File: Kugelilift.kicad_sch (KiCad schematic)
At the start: 14 parts, among them J1 I2C, J2 TTL, J4 Stepper, SW1 RESET, SW2 MODE, U1 magnetic-charger, U2 TCRT5000, U3 ULN2003A, U4 esp-01f, U5 UA78M33_TO252

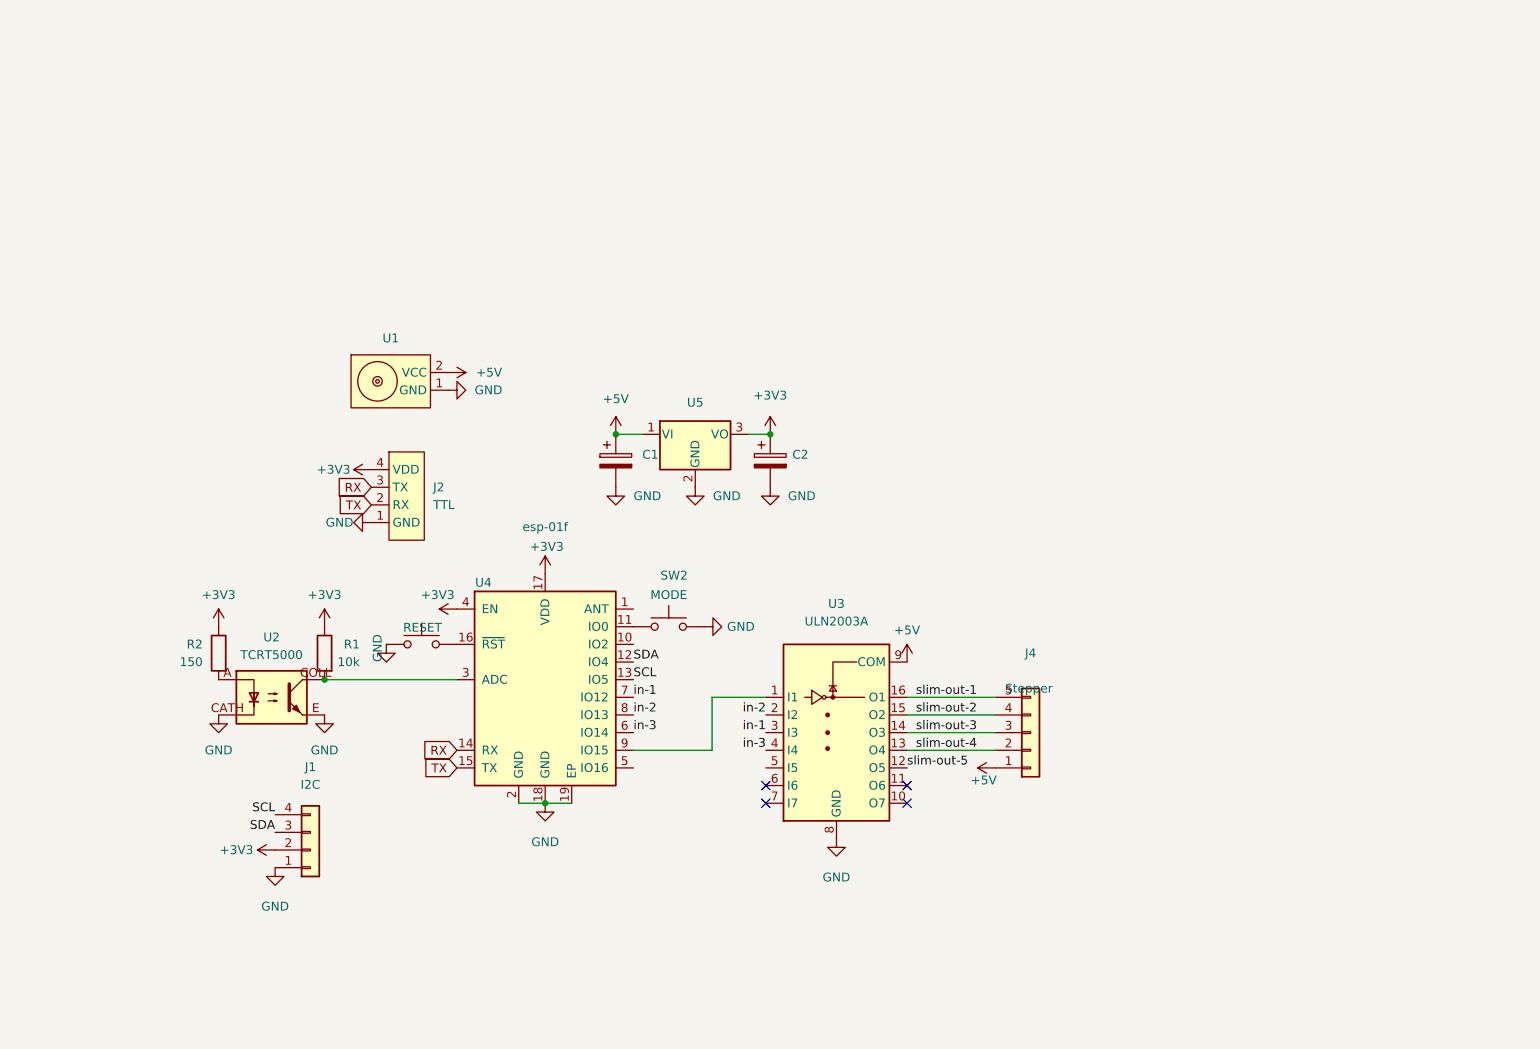
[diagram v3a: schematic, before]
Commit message: PCB based on ESP01m
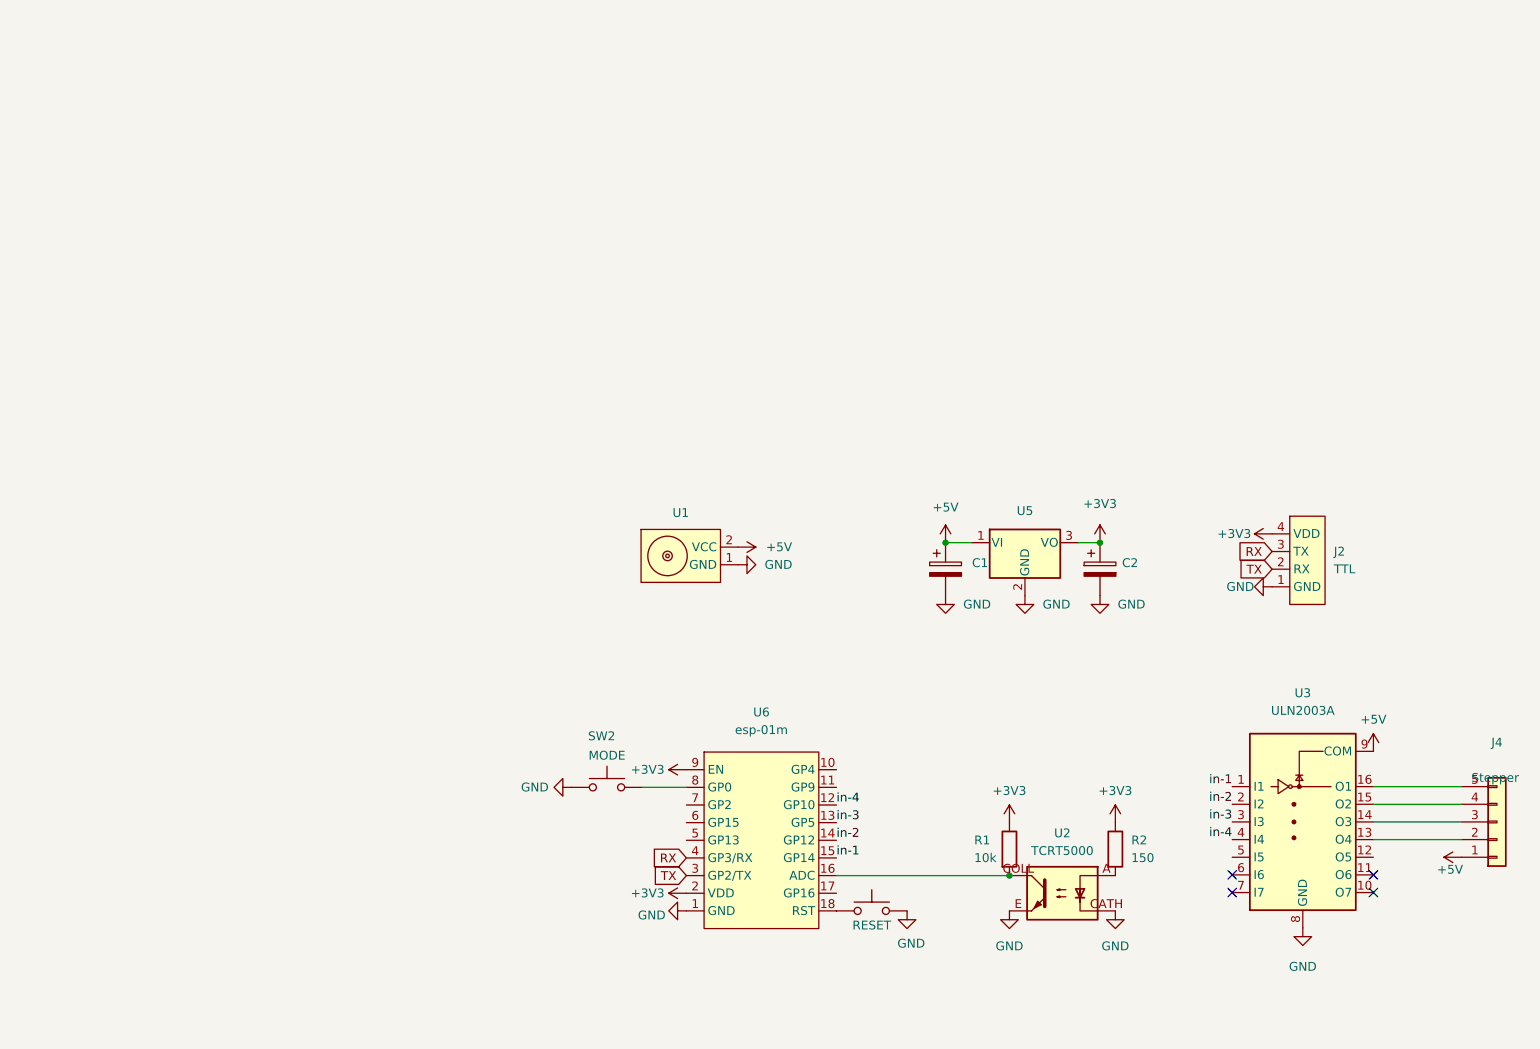
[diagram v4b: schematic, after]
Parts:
- removed J1: I2C, Connector_PinHeader_2.54mm:PinHeader_1x04_P2.54mm_Vertical, symbol Connector_Generic:Conn_01x04
- removed U4: esp-01f, esp-01f:esp-01f, symbol esp-01f:esp-01f
- added U6: esp-01m, esp-01m:esp-01m, symbol esp-01m:esp-01m
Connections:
- net +3V3: now also U6.2 (VDD), U6.9 (EN)
- net GND: now also U6.1 (GND)
- net RX: now also U6.4 (GP3/RX)
- net TX: now also U6.3 (GP2/TX)
- net in-1: now also U3.1 (I1), U6.15 (GP14); no longer U3.3 (I3)
- net in-2: now also U6.14 (GP12)
- net in-3: now also U3.3 (I3), U6.13 (GP5); no longer U3.4 (I4)
- net at SW2.1: now also U6.8 (GP0)
- net at SW1.1: now also U6.18 (RST)
- net at R1.2, U2.COLL: now also U6.16 (ADC)
- net slim-out-1: no longer names the net of J4.5 (Pin_5), U3.16 (O1)
- net slim-out-2: no longer names the net of J4.4 (Pin_4), U3.15 (O2)
- net slim-out-3: no longer names the net of J4.3 (Pin_3), U3.14 (O3)
- net slim-out-4: no longer names the net of J4.2 (Pin_2), U3.13 (O4)
- net slim-out-5: no longer names the net of U3.12 (O5)
- new net in-4: U3.4 (I4), U6.12 (GP10)
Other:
- moved on the sheet: C1, C2, J2, J4, R1, R2, SW2, U1, U2, U3, U5

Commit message: Prepare for next iteration
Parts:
- added SW3, SW?: SW_Push, Button_Switch_SMD:SW_Push_1P1T_NO_CK_KMR2, symbol Switch:SW_Push
- added SW4: SW_DIP_x04, Button_Switch_THT:SW_DIP_SPSTx04_Slide_6.7x11.72mm_W7.62mm_P2.54mm_LowProfile, symbol Switch:SW_DIP_x04
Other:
- note added: "TODOS: - Two user buttons for manual operation or configuration at startup - IR Receiver mode for use with a remote control. (needs a POC) - DIP Switches on the underside for configuration / wifi-enable etc. - Battery module adapter using magnetic sockets + uart (i2c)"
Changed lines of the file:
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@@
     (stroke (width 0) (type default) (color 0 0 0 0))
+  )
+  (text "TODOS:\n\n- Two user buttons for manual operation or configuration at startup\n- IR Receiver mode for use with a remote control. (needs a POC)\n- DIP Switches on the underside for configuration / wifi-enable etc.\n- Battery module adapter using magnetic sockets + uart (i2c)"
+    (at 33.02 93.98 0)
+    (effects (font (size 1.27 1.27)) (justify left bottom))
   )
   (label "in-4" (at 191.5668 129.4384 180)
@@
     (pin "1")
   )
+  (symbol (lib_id "Switch:SW_Push") (at 35.56 120.65 0) (unit 1)
+    (in_bom yes) (on_board yes) (fields_autoplaced)
+    (property "Reference" "SW3" (id 0) (at 35.56 113.03 0))
+    (property "Value" "SW_Push" (id 1) (at 35.56 115.57 0))
+    (property "Footprint" "Button_Switch_SMD:SW_Push_1P1T_NO_CK_KMR2" (id 2) (at 35.56 115.57 0)
+      (effects (font (size 1.27 1.27)) hide)
+    )
+    (property "Datasheet" "~" (id 3) (at 35.56 115.57 0)
+      (effects (font (size 1.27 1.27)) hide)
+    )
+    (pin "1")
+    (pin "2")
+  )
   (symbol (lib_id "power:GND") (at 120.4722 89.8906 90) (unit 1)
     (in_bom yes) (on_board yes) (fields_autoplaced)
@@
     )
     (pin "1")
+  )
+  (symbol (lib_id "Switch:SW_Push") (at 35.56 133.35 0) (unit 1)
+    (in_bom yes) (on_board yes) (fields_autoplaced)
+    (property "Reference" "SW?" (id 0) (at 35.56 125.73 0))
+    (property "Value" "SW_Push" (id 1) (at 35.56 128.27 0))
+    (property "Footprint" "Button_Switch_SMD:SW_Push_1P1T_NO_CK_KMR2" (id 2) (at 35.56 128.27 0)
+      (effects (font (size 1.27 1.27)) hide)
+    )
+    (property "Datasheet" "~" (id 3) (at 35.56 128.27 0)
+      (effects (font (size 1.27 1.27)) hide)
+    )
+    (pin "1")
+    (pin "2")
   )
   (symbol (lib_id "Device:C_Polarized") (at 172.5422 90.5256 0) (unit 1)
@@
     (pin "1")
   )
+  (symbol (lib_id "Switch:SW_DIP_x04") (at 72.39 152.4 0) (unit 1)
+    (in_bom yes) (on_board yes) (fields_autoplaced)
+    (property "Reference" "SW4" (id 0) (at 72.39 139.7 0))
+    (property "Value" "SW_DIP_x04" (id 1) (at 72.39 142.24 0))
+    (property "Footprint" "Button_Switch_THT:SW_DIP_SPSTx04_Slide_6.7x11.72mm_W7.62mm_P2.54mm_LowProfile" (id 2) (at 72.39 152.4 0)
+      (effects (font (size 1.27 1.27)) hide)
+    )
+    (property "Datasheet" "~" (id 3) (at 72.39 152.4 0)
+      (effects (font (size 1.27 1.27)) hide)
+    )
+    (pin "1")
+    (pin "2")
+    (pin "3")
+    (pin "4")
+    (pin "5")
+    (pin "6")
+    (pin "7")
+    (pin "8")
+  )
   (symbol (lib_id "Device:R") (at 159.512 130.81 0) (unit 1)
     (in_bom yes) (on_board yes)
@@
       (reference "SW2") (unit 1) (value "MODE") (footprint "Connector_PinHeader_2.54mm:PinHeader_1x03_P2.54mm_Vertical")
     )
+    (path "/b13fa82f-cdd3-4be6-ab58-37de420aaa9d"
+      (reference "SW3") (unit 1) (value "SW_Push") (footprint "Button_Switch_SMD:SW_Push_1P1T_NO_CK_KMR2")
+    )
+    (path "/e42a20e3-d566-4bf6-9ee2-1184d2a0b9e2"
+      (reference "SW4") (unit 1) (value "SW_DIP_x04") (footprint "Button_Switch_THT:SW_DIP_SPSTx04_Slide_6.7x11.72mm_W7.62mm_P2.54mm_LowProfile")
+    )
+    (path "/b4775607-23b7-46a7-bffc-efa9cfbadee3"
+      (reference "SW?") (unit 1) (value "SW_Push") (footprint "Button_Switch_SMD:SW_Push_1P1T_NO_CK_KMR2")
+    )
     (path "/de79cc46-5f96-419e-9bf0-8ae3ec6188f1"
